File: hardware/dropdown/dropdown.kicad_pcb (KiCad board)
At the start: 2 copper layers, 20.8 x 10 mm, 14 parts, among them J1 12, J2 G, J3 3, J4 G, J5 12, J6 G, J7 3, J8 G, T1 T1, T2 T2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

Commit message: feat: drop down 4 layer
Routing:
- net (no net): vias 0 -> 3
- added copper zone on In2.Cu, net +12V
- added copper zone on In1.Cu, net +3.3V
- added copper zone on B.Cu, net GND
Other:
- copper layers 2 -> 4
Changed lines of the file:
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@@
   (layers
     (0 "F.Cu" signal)
+    (1 "In1.Cu" power)
+    (2 "In2.Cu" signal)
     (31 "B.Cu" signal)
     (32 "B.Adhes" user "B.Adhesive")
@@
       (layer "F.Mask" (type "Top Solder Mask") (thickness 0.01))
       (layer "F.Cu" (type "copper") (thickness 0.035))
-      (layer "dielectric 1" (type "core") (thickness 1.51) (material "FR4") (epsilon_r 4.5) (loss_tangent 0.02))
+      (layer "dielectric 1" (type "core") (thickness 0.1) (material "FR4") (epsilon_r 4.5) (loss_tangent 0.02))
+      (layer "In1.Cu" (type "copper") (thickness 0.035))
+      (layer "dielectric 2" (type "core") (thickness 1.24) (material "FR4") (epsilon_r 4.5) (loss_tangent 0.02))
+      (layer "In2.Cu" (type "copper") (thickness 0.035))
+      (layer "dielectric 3" (type "prepreg") (thickness 0.1) (material "FR4") (epsilon_r 4.5) (loss_tangent 0.02))
       (layer "B.Cu" (type "copper") (thickness 0.035))
       (layer "B.Mask" (type "Bottom Solder Mask") (thickness 0.01))
@@
       (net 1 "+3.3V") (pinfunction "Pin_1") (pintype "passive"))
   )
+  (gr_poly
+    (pts
+      (xy 73.1 61)
+      (xy 76.8 61)
+      (xy 76.8 62.3)
+      (xy 76.15 62.3)
+      (xy 75.85 62.6)
+      (xy 73.1 62.6)
+    )
+    (stroke (width 0.2) (type solid)) (fill solid) (layer "F.Cu"))
+  (gr_poly
+    (pts
+      (xy 77.65 58.95)
+      (xy 86.65 58.95)
+      (xy 86.65 63.75)
+      (xy 86.3 63.75)
+      (xy 85.5 62.95)
+      (xy 85.55 62.95)
+      (xy 85.5 63)
+      (xy 81.8 63)
+      (xy 79.7 60.9)
+      (xy 79.7 60.85)
+      (xy 79.6 60.75)
+      (xy 77.7 60.75)
+      (xy 77.65 60.7)
+    )
+    (stroke (width 0.2) (type solid)) (fill solid) (layer "F.Cu"))
+  (gr_poly
+    (pts
+      (xy 73.15 64.4)
+      (xy 75.2 64.4)
+      (xy 75.2 64.85)
+      (xy 75.25 64.9)
+      (xy 76.85 64.9)
+      (xy 76.85 66.3)
+      (xy 76.8 66.35)
+      (xy 73.15 66.35)
+    )
+    (stroke (width 0.2) (type solid)) (fill solid) (layer "F.Cu"))
+  (gr_poly
+    (pts
+      (xy 90.4 65.5)
+      (xy 91.5 65.5)
+      (xy 91.5 66.5)
+      (xy 90.4 66.5)
+    )
+    (stroke (width 0.2) (type solid)) (fill solid) (layer "F.Cu"))
+  (gr_poly
+    (pts
+      (xy 87.05 58.5)
+      (xy 92.25 58.5)
+      (xy 92.25 60.3)
+      (xy 92.15 60.4)
+      (xy 90.15 60.4)
+      (xy 90.15 62.3)
+      (xy 90.1 62.35)
+      (xy 87.05 62.35)
+    )
+    (stroke (width 0.2) (type solid)) (fill solid) (layer "F.Cu"))
+  (gr_poly
+    (pts
+      (xy 81.4 66.4)
+      (xy 90.3 66.4)
+      (xy 90.3 64.05)
+      (xy 90.2 63.95)
+      (xy 87.675 63.95)
+      (xy 86.775 64.85)
+      (xy 83.65 64.85)
+      (xy 83.35 65.15)
+      (xy 81.35 65.15)
+      (xy 81.35 66.35)
+    )
+    (stroke (width 0.2) (type solid)) (fill solid) (layer "F.Cu"))
+  (gr_poly
+    (pts
+      (xy 87.15 62.2)
+      (xy 90 62.2)
+      (xy 90 60.15)
+      (xy 90.6 59.55)
+      (xy 90.6 58.75)
+      (xy 90.55 58.7)
+      (xy 87.15 58.7)
+    )
+    (stroke (width 0.2) (type solid)) (fill solid) (layer "F.Cu"))
+  (gr_poly
+    (pts
+      (xy 83.05 65.05)
+      (xy 83.05 64.75)
+      (xy 83.65 64.75)
+      (xy 83.35 65.05)
+    )
+    (stroke (width 0.2) (type solid)) (fill solid) (layer "F.Cu"))
   (gr_rect (start 72.95 58.25) (end 93.8 68.25)
     (stroke (width 0.1) (type default)) (fill none) (layer "Edge.Cuts"))
+  (via blind (at 91 66.05) (size 0.8) (drill 0.4) (layers "F.Cu" "In2.Cu") (net 0))
+  (via blind (at 91.6 59.45) (size 0.8) (drill 0.4) (layers "F.Cu" "In1.Cu") (net 0))
+  (via blind (at 78.35 59.9) (size 0.8) (drill 0.4) (layers "F.Cu" "B.Cu") (net 0))
   (segment (start 89.95 59.4) (end 87.9 59.4) (width 1) (layer "F.Cu") (net 1))
   (segment (start 89.35 61.5) (end 89.35 60) (width 1) (layer "F.Cu") (net 1))
@@
   (segment (start 89.35 60) (end 89.95 59.4) (width 1) (layer "F.Cu") (net 1))
   (segment (start 87.675 61.5) (end 89.35 61.5) (width 1) (layer "F.Cu") (net 1))
+  (segment (start 83.05 60.65) (end 83.075 60.65) (width 1) (layer "F.Cu") (net 2))
   (segment (start 79.8 59.8) (end 80.125 59.8) (width 0.5) (layer "F.Cu") (net 2))
   (segment (start 80.125 59.8) (end 82.025 61.7) (width 1) (layer "F.Cu") (net 2))
@@
   (segment (start 84.05 59.8) (end 84.05 61.85) (width 1) (layer "F.Cu") (net 2))
   (segment (start 86.125 61.5) (end 86.125 62.775) (width 1) (layer "F.Cu") (net 2))
+  (segment (start 83.075 60.65) (end 83.925 59.8) (width 1) (layer "F.Cu") (net 2))
   (segment (start 81.85 59.8) (end 84.05 59.8) (width 1) (layer "F.Cu") (net 2))
   (segment (start 82.025 59.975) (end 81.85 59.8) (width 0.25) (layer "F.Cu") (net 2))
   (segment (start 86.125 62.775) (end 86.55 63.2) (width 1) (layer "F.Cu") (net 2))
   (segment (start 84.05 61.85) (end 85.775 61.85) (width 1) (layer "F.Cu") (net 2))
-  (segment (start 82.025 61.7) (end 83.925 59.8) (width 1) (layer "F.Cu") (net 2))
+  (segment (start 82.025 61.7) (end 83.05 60.675) (width 1) (layer "F.Cu") (net 2))
   (segment (start 89.2375 63.2) (end 89.4375 63) (width 1) (layer "F.Cu") (net 2))
   (segment (start 82.175 61.85) (end 82.025 61.7) (width 0.25) (layer "F.Cu") (net 2))
   (segment (start 82.025 61.7) (end 82.025 59.975) (width 1) (layer "F.Cu") (net 2))
   (segment (start 86.55 63.2) (end 87.65 63.2) (width 1) (layer "F.Cu") (net 2))
+  (segment (start 83.05 60.675) (end 83.05 60.65) (width 1) (layer "F.Cu") (net 2))
   (segment (start 87 65.4) (end 87 65.45) (width 0.25) (layer "F.Cu") (net 3))
   (segment (start 87.65 64.75) (end 87 65.4) (width 1) (layer "F.Cu") (net 3))
@@
   (segment (start 74.1 62) (end 75.775 62) (width 1) (layer "F.Cu") (net 5))
   (segment (start 75.775 62) (end 76.075 61.7) (width 1) (layer "F.Cu") (net 5))
+  (zone (net 1) (net_name "+3.3V") (layer "In1.Cu") (hatch full 0.5)
+    (connect_pads (clearance 0.5))
+    (min_thickness 0.25) (filled_areas_thickness no)
+    (fill yes (thermal_gap 0.5) (thermal_bridge_width 0.5))
+    (polygon
+      (pts
+        (xy 73 58.3)
+        (xy 93.75 58.3)
+        (xy 93.75 68.2)
+        (xy 73 68.2)
+      )
+    )
+  )
+  (zone (net 4) (net_name "+12V") (layer "In2.Cu") (hatch full 0.5)
+    (priority 1)
+    (connect_pads (clearance 0.5))
+    (min_thickness 0.25) (filled_areas_thickness no)
+    (fill yes (thermal_gap 0.5) (thermal_bridge_width 0.5))
+    (polygon
+      (pts
+        (xy 73 58.3)
+        (xy 93.7 58.3)
+        (xy 93.75 58.35)
+        (xy 93.75 68.15)
+        (xy 73.05 68.15)
+        (xy 73 68.1)
+      )
+    )
+  )
+  (zone (net 2) (net_name "GND") (layer "B.Cu") (hatch full 0.5)
+    (priority 2)
+    (connect_pads (clearance 0.5))
+    (min_thickness 0.25) (filled_areas_thickness no)
+    (fill yes (thermal_gap 0.5) (thermal_bridge_width 0.5))
+    (polygon
+      (pts
+        (xy 76.05 58.3)
+        (xy 86.2 58.3)
+        (xy 86.2 63.85)
+        (xy 86.1 63.95)
+        (xy 76.05 63.95)
+      )
+    )
+  )
 )

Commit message: ams1117
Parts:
- removed J5: 12, TestPoint:TestPoint_THTPad_1.0x1.0mm_Drill0.5mm
- added C3: 100nF, Capacitor_SMD:C_0603_1608Metric, F.Cu at (83.8, 64.1)
- added C4: 100nF, Capacitor_SMD:C_0603_1608Metric, F.Cu at (84.5, 60.2)
- J1, J2, J3, J4, J6, J7, J8, T1, T2: footprint TestPoint:TestPoint_THTPad_1.0x1.0mm_Drill0.5mm -> TestPoint:TestPoint_THTPad_1.5x1.5mm_Drill0.7mm
- U2: value AP7381-33Y-13 -> AMS1117-3.3
- moved J6 9.87 mm to (74.2, 60.7)
- moved J2 3.18 mm to (76.8, 60.7)
- moved J8 2.75 mm to (79.2, 60.7)
- moved J4 2.47 mm to (81.8, 60.7)
- moved U2 2.46 mm to (89.3, 64.5)
- moved C2 2.40 mm to (85.2, 64.1)
- moved C1 2.39 mm to (84.5, 61.8)
- moved T2 1.86 mm to (74.2, 63.9)
- moved D3 1.66 mm to (79.2, 65.3)
- moved J1 1.47 mm to (84.2, 66.8)
- moved T1 1.40 mm to (74.2, 66.8)
- moved J7 0.63 mm to (87.3, 59.6)
- moved J3 0.22 mm to (89.8, 59.6)
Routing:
- net GND: track 23.3 -> 0.00 mm, vias 0 -> 3
- net +3.3V: track 8.27 -> 0.00 mm, vias 0 -> 2
- net VD: track 7.85 -> 0.00 mm, vias 0 -> 2
- net GND1: track 2.10 -> 0.00 mm
- net +12V: track 2.03 -> 0.00 mm
- net (no net): vias 3 -> 0
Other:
- board size 20.8 x 10 mm -> 19 x 10 mm

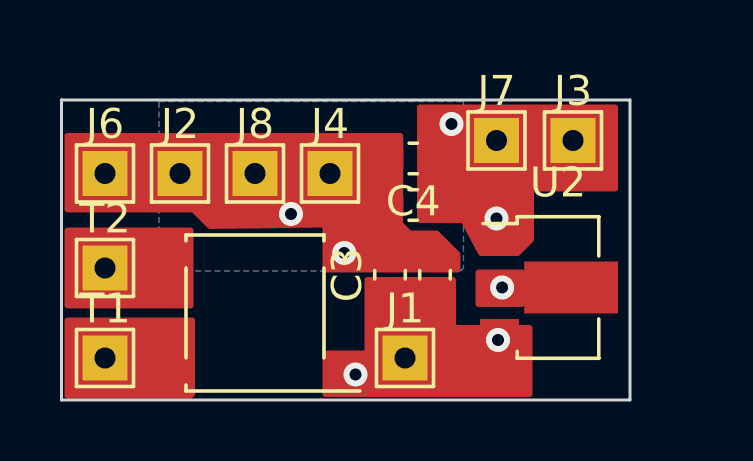
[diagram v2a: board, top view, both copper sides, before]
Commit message: fix: apply jlcpcb rules (#18)
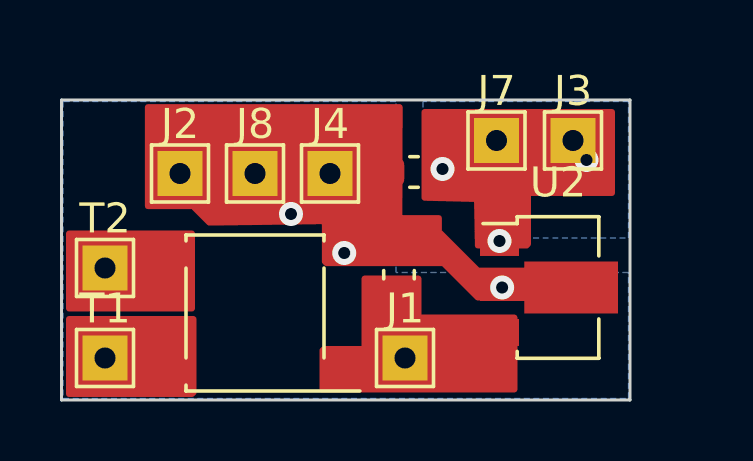
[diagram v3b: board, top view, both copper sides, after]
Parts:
- removed C3, C4: 100nF, Capacitor_SMD:C_0603_1608Metric
- removed J6: G, TestPoint:TestPoint_THTPad_1.5x1.5mm_Drill0.7mm
- moved C2 1.20 mm to (84.0, 64.1)
- moved C1 1.10 mm to (84.5, 60.6)
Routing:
- net GND: track 0.00 -> 16.1 mm
- net +3.3V: track 0.00 -> 8.40 mm, vias 2 -> 3
- net VD: track 0.00 -> 7.82 mm, vias 2 -> 0
- net GND1: track 0.00 -> 2.23 mm
- net +12V: track 0.00 -> 2.23 mm
- added copper zone on B.Cu, net +3.3V
- removed copper zone on In2.Cu, net +12V
- removed copper zone on In1.Cu, net +3.3V
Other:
- copper layers 4 -> 2
